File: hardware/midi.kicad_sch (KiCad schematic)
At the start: 13 parts, among them J16 MIDI_OUT, J19 MIDI_IN, U13 H11L1

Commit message: Reset references and remove THT footprint assignments.
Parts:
- C70: footprint Capacitor_THT:C_Rect_L4.0mm_W2.5mm_P2.50mm -> (none)
- D5: footprint Diode_THT:D_DO-35_SOD27_P2.54mm_Vertical_AnodeUp -> (none)
- D6, D7: footprint LED_THT:LED_D3.0mm -> (none)
- R64: renamed from R58; footprint Resistor_THT:R_Axial_DIN0207_L6.3mm_D2.5mm_P2.54mm_Vertical -> (none)
- R65: renamed from R59; footprint Resistor_THT:R_Axial_DIN0207_L6.3mm_D2.5mm_P2.54mm_Vertical -> (none)
- R66: renamed from R60; footprint Resistor_THT:R_Axial_DIN0207_L6.3mm_D2.5mm_P2.54mm_Vertical -> (none)
- R67: renamed from R61; footprint Resistor_THT:R_Axial_DIN0207_L6.3mm_D2.5mm_P2.54mm_Vertical -> (none)
- R68: renamed from R62; footprint Resistor_THT:R_Axial_DIN0207_L6.3mm_D2.5mm_P2.54mm_Vertical -> (none)
- R69: renamed from R63; footprint Resistor_THT:R_Axial_DIN0207_L6.3mm_D2.5mm_P2.54mm_Vertical -> (none)
- U13: footprint Package_DIP:DIP-6_W7.62mm -> Package_DIP:SMDIP-6_W9.53mm
- renumbered J19 to J16, J16 to J17
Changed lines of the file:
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@@
 		(on_board yes)
 		(dnp no)
-		(property "Reference" "R59"
+		(property "Reference" "R65"
 			(at 107.95 77.47 0)
 			(effects
@@
 			)
 		)
-		(property "Footprint" "Resistor_THT:R_Axial_DIN0207_L6.3mm_D2.5mm_P2.54mm_Vertical"
+		(property "Footprint" ""
 			(at 104.902 78.74 90)
 			(effects
@@
 			(project "Zero-Stomp"
 				(path "/8c8d5801-9c58-4283-98ac-c6a8e7250e15/853950ce-5a52-4886-be78-90306209bbaa"
-					(reference "R59")
+					(reference "R65")
 					(unit 1)
 				)
@@
 		(on_board yes)
 		(dnp no)
-		(property "Reference" "R62"
+		(property "Reference" "R68"
 			(at 175.26 95.25 90)
 			(effects
@@
 			)
 		)
-		(property "Footprint" "Resistor_THT:R_Axial_DIN0207_L6.3mm_D2.5mm_P2.54mm_Vertical"
+		(property "Footprint" ""
 			(at 175.26 90.932 90)
 			(effects
@@
 			(project "Zero-Stomp"
 				(path "/8c8d5801-9c58-4283-98ac-c6a8e7250e15/853950ce-5a52-4886-be78-90306209bbaa"
-					(reference "R62")
+					(reference "R68")
 					(unit 1)
 				)
@@
 			)
 		)
-		(property "Footprint" "LED_THT:LED_D3.0mm"
+		(property "Footprint" ""
 			(at 114.3 87.63 0)
 			(effects
@@
 		(dnp no)
 		(fields_autoplaced yes)
-		(property "Reference" "J19"
+		(property "Reference" "J16"
 			(at 68.58 86.36 0)
 			(effects
@@
 			(project "Zero-Stomp"
 				(path "/8c8d5801-9c58-4283-98ac-c6a8e7250e15/853950ce-5a52-4886-be78-90306209bbaa"
-					(reference "J19")
+					(reference "J16")
 					(unit 1)
 				)
@@
 			)
 		)
-		(property "Footprint" "Package_DIP:DIP-6_W7.62mm"
+		(property "Footprint" "Package_DIP:SMDIP-6_W9.53mm"
 			(at 96.774 92.71 0)
 			(effects
@@
 		(dnp no)
 		(fields_autoplaced yes)
-		(property "Reference" "J16"
+		(property "Reference" "J17"
 			(at 189.23 91.4399 0)
 			(effects
@@
 			(project ""
 				(path "/8c8d5801-9c58-4283-98ac-c6a8e7250e15/853950ce-5a52-4886-be78-90306209bbaa"
-					(reference "J16")
+					(reference "J17")
 					(unit 1)
 				)
@@
 		(on_board yes)
 		(dnp no)
-		(property "Reference" "R63"
+		(property "Reference" "R69"
 			(at 181.61 77.47 0)
 			(effects
@@
 			)
 		)
-		(property "Footprint" "Resistor_THT:R_Axial_DIN0207_L6.3mm_D2.5mm_P2.54mm_Vertical"
+		(property "Footprint" ""
 			(at 178.562 78.74 90)
 			(effects
@@
 			(project "Zero-Stomp"
 				(path "/8c8d5801-9c58-4283-98ac-c6a8e7250e15/853950ce-5a52-4886-be78-90306209bbaa"
-					(reference "R63")
+					(reference "R69")
 					(unit 1)
 				)
@@
 			)
 		)
-		(property "Footprint" "Diode_THT:D_DO-35_SOD27_P2.54mm_Vertical_AnodeUp"
+		(property "Footprint" ""
 			(at 85.09 92.71 0)
 			(effects
@@
 			)
 		)
-		(property "Footprint" "Capacitor_THT:C_Rect_L4.0mm_W2.5mm_P2.50mm"
+		(property "Footprint" ""
 			(at 91.7448 81.28 0)
 			(effects
@@
 		(on_board yes)
 		(dnp no)
-		(property "Reference" "R60"
+		(property "Reference" "R66"
 			(at 115.57 80.01 0)
 			(effects
@@
 			)
 		)
-		(property "Footprint" "Resistor_THT:R_Axial_DIN0207_L6.3mm_D2.5mm_P2.54mm_Vertical"
+		(property "Footprint" ""
 			(at 116.078 78.74 90)
 			(effects
@@
 			(project "Zero-Stomp"
 				(path "/8c8d5801-9c58-4283-98ac-c6a8e7250e15/853950ce-5a52-4886-be78-90306209bbaa"
-					(reference "R60")
+					(reference "R66")
 					(unit 1)
 				)
@@
 		(on_board yes)
 		(dnp no)
-		(property "Reference" "R61"
+		(property "Reference" "R67"
 			(at 170.18 77.47 0)
 			(effects
@@
 			)
 		)
-		(property "Footprint" "Resistor_THT:R_Axial_DIN0207_L6.3mm_D2.5mm_P2.54mm_Vertical"
+		(property "Footprint" ""
 			(at 167.132 78.74 90)
 			(effects
@@
 			(project "Zero-Stomp"
 				(path "/8c8d5801-9c58-4283-98ac-c6a8e7250e15/853950ce-5a52-4886-be78-90306209bbaa"
-					(reference "R61")
+					(reference "R67")
 					(unit 1)
 				)
@@
 			)
 		)
-		(property "Footprint" "LED_THT:LED_D3.0mm"
+		(property "Footprint" ""
 			(at 168.91 87.63 0)
 			(effects
@@
 		(on_board yes)
 		(dnp no)
-		(property "Reference" "R58"
+		(property "Reference" "R64"
 			(at 77.47 90.424 90)
 			(effects
@@
 			)
 		)
-		(property "Footprint" "Resistor_THT:R_Axial_DIN0207_L6.3mm_D2.5mm_P2.54mm_Vertical"
+		(property "Footprint" ""
 			(at 77.47 90.932 90)
 			(effects
@@
 			(project "Zero-Stomp"
 				(path "/8c8d5801-9c58-4283-98ac-c6a8e7250e15/853950ce-5a52-4886-be78-90306209bbaa"
-					(reference "R58")
-					(unit 1)
-				)
+					(reference "R64")
+					(unit 1)
+				)

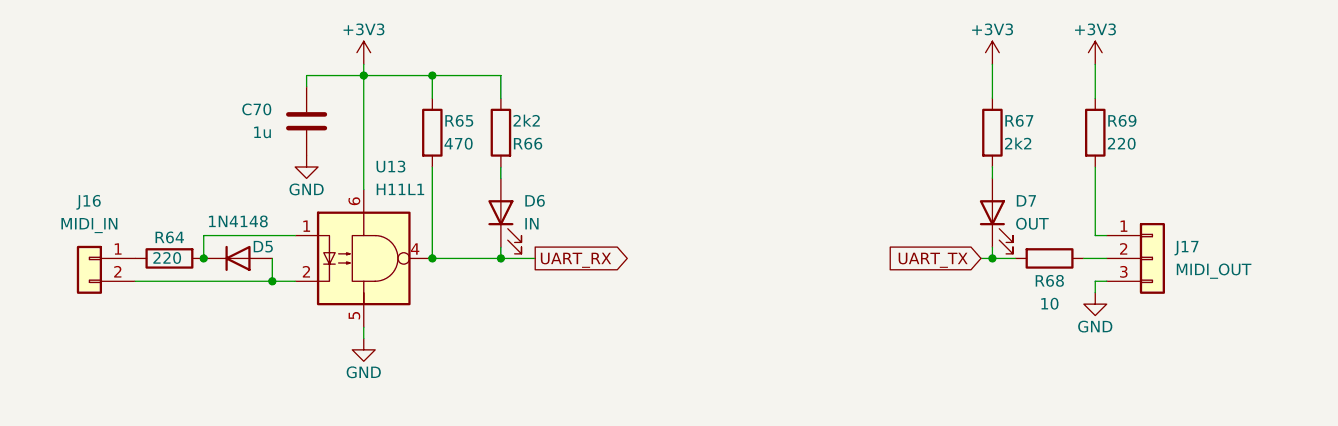
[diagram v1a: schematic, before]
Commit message: Footprint assignments
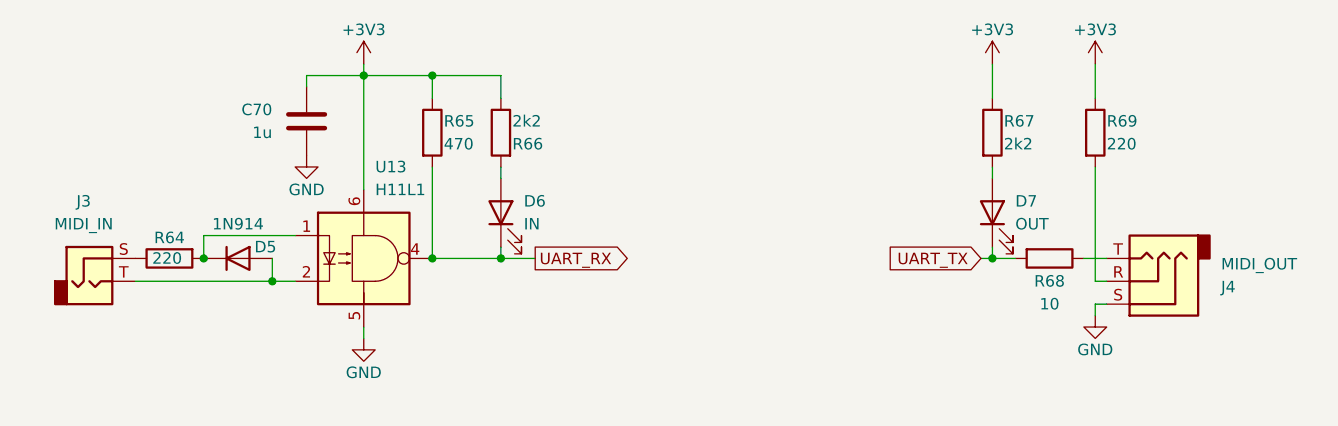
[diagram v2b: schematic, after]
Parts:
- removed D5: 1N4148, symbol Diode:1N4148
- removed J16: MIDI_IN, symbol Connector_Generic:Conn_01x02
- removed J17: MIDI_OUT, symbol Connector_Generic:Conn_01x03
- added D5: 1N914, Diode_SMD:D_SOD-123, symbol Diode:1N914
- added J3: MIDI_IN, Connector_JST:JST_PH_B2B-PH-K_1x02_P2.00mm_Vertical, symbol Connector_Audio:AudioJack2
- added J4: MIDI_OUT, Connector_JST:JST_PH_B3B-PH-K_1x03_P2.00mm_Vertical, symbol Connector_Audio:AudioJack3
- C70: footprint (none) -> Capacitor_SMD:C_0603_1608Metric
- D6, D7: footprint (none) -> LED_SMD:LED_0603_1608Metric
- R64, R65, R66, R67, R69: footprint (none) -> Resistor_SMD:R_0603_1608Metric
- R68: footprint (none) -> Resistor_SMD:R_0805_2012Metric
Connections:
- net GND: now also J4.S
- net at R68.1: now also J4.T
- net at R64.1: now also J3.S
- net at U13.2: now also D5.2 (A), J3.T
- net at R64.2, U13.1: now also D5.1 (K)
- net at R69.2: now also J4.R

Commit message: Change connectors to JST SH
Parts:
- J3: footprint Connector_JST:JST_PH_B2B-PH-K_1x02_P2.00mm_Vertical -> Connector_JST:JST_SH_SM02B-SRSS-TB_1x02-1MP_P1.00mm_Horizontal
- J4: footprint Connector_JST:JST_PH_B3B-PH-K_1x03_P2.00mm_Vertical -> Connector_JST:JST_SH_SM03B-SRSS-TB_1x03-1MP_P1.00mm_Horizontal
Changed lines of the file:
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@@
 			)
 		)
-		(property "Footprint" "Connector_JST:JST_PH_B2B-PH-K_1x02_P2.00mm_Vertical"
+		(property "Footprint" "Connector_JST:JST_SH_SM02B-SRSS-TB_1x02-1MP_P1.00mm_Horizontal"
 			(at 68.58 95.25 0)
 			(effects
@@
 			)
 		)
-		(property "Footprint" "Connector_JST:JST_PH_B3B-PH-K_1x03_P2.00mm_Vertical"
+		(property "Footprint" "Connector_JST:JST_SH_SM03B-SRSS-TB_1x03-1MP_P1.00mm_Horizontal"
 			(at 186.69 95.25 0)
 			(effects

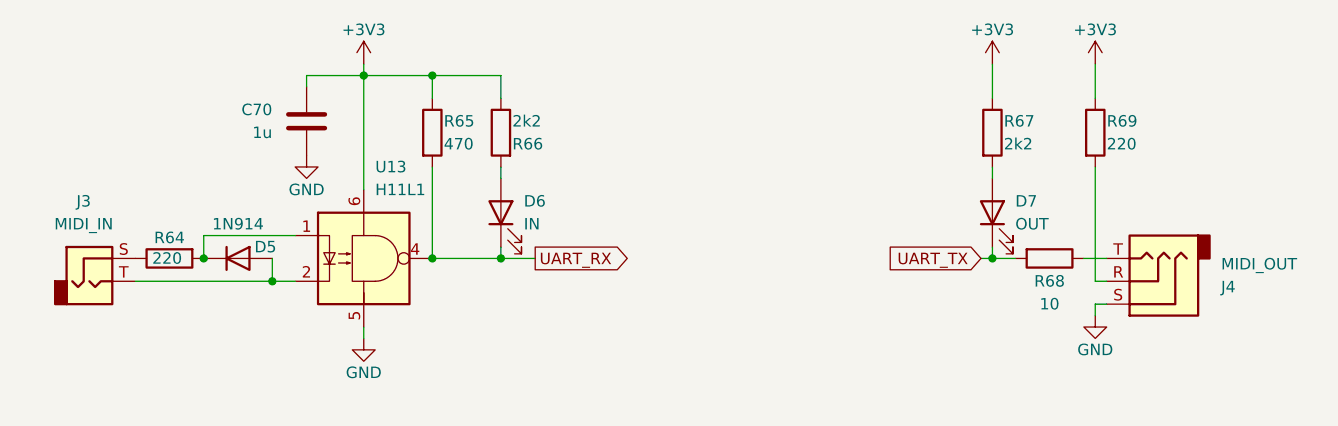
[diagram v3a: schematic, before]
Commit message: Change out H11L1 with TLP2362
For smaller footprint!
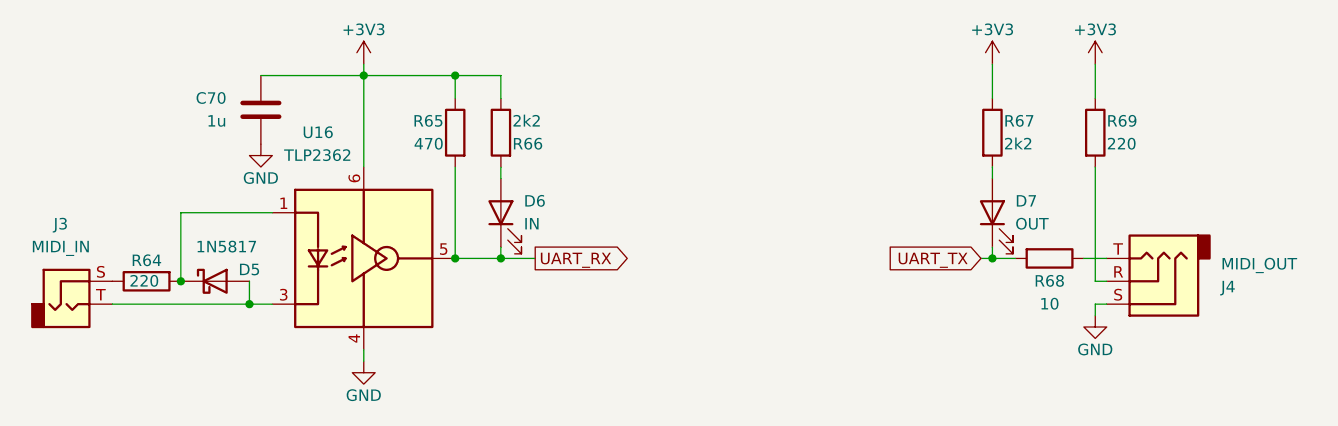
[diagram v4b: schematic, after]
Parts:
- removed D5: 1N914, Diode_SMD:D_SOD-123, symbol Diode:1N914
- removed U13: H11L1, Package_DIP:SMDIP-6_W9.53mm, symbol Isolator:H11L1
- added D5: 1N5817, Diode_SMD:D_SOD-123, symbol Diode:1N5817
- added U16: TLP2362, Package_SO:SO-5-6_4.55x3.7mm_P1.27mm, symbol Zero-Stomp:TLP2362
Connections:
- net +3V3: now also U16.6 (VDD)
- net GND: now also U16.4 (GND)
- net UART_RX: now also U16.5 (VO)
- net at J3.T: now also D5.2 (A), U16.3 (K)
- net at R64.2: now also D5.1 (K), U16.1 (A)
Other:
- moved on the sheet: C70, J3, R64, R65
